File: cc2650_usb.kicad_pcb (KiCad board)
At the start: 2 copper layers, 49.9 x 28 mm, 63 parts, among them P1 CONN_01X07, P2 CONN_01X04, P3 CONN_01X02, P4 CONN_01X08, U1 CC2650F128RHB, X1 24Mhz, Y1 32.768kHz

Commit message: More routing
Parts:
- added C18: 1uF, Capacitors_SMD:C_0603, F.Cu at (141.2, 110.5)
- added C19: 1uF, Capacitors_SMD:C_0603, F.Cu at (146.1, 108.7)
- added D1: USR_LED, LEDs:LED_0603, F.Cu at (120.0, 62.0)
- added D2: PWR_LED, LEDs:LED_0603, F.Cu at (138.6, 108.1)
- added D3: BAT60JFILM, Diodes_SMD:SOD-323, F.Cu at (145.4, 106.3)
- added P5: VBAT, battery_extra:CR2032_SMD, B.Cu at (152.7, 105.1)
- added Q1: FDN340P, TO_SOT_Packages_SMD:SOT-23, F.Cu at (141.6, 105.4)
- added R3: 360R, Resistors_SMD:R_0603, F.Cu at (113.0, 68.2)
- added R4: 360R, Resistors_SMD:R_0603, F.Cu at (138.6, 105.2)
- added R5: 100K, Resistors_SMD:R_0603, F.Cu at (111.9, 82.7)
- added REF**: VIA_0.6mm, GNDVIA:GND_VIA_0.6mm, F.Cu at (146.5, 90.1)
- added REF**: VIA_0.6mm, GNDVIA:GND_VIA_0.6mm, F.Cu at (148.3, 105.3)
- added REF**: VIA_0.6mm, GNDVIA:GND_VIA_0.6mm, F.Cu at (154.5, 90.1)
- added REF**: VIA_0.6mm, GNDVIA:GND_VIA_0.6mm, F.Cu at (168.0, 99.2)
- added REF**: VIA_0.6mm, GNDVIA:GND_VIA_0.6mm, F.Cu at (166.9, 99.2)
- added REF**: VIA_0.6mm, GNDVIA:GND_VIA_0.6mm, F.Cu at (165.7, 99.2)
- added REF**: VIA_0.6mm, GNDVIA:GND_VIA_0.6mm, F.Cu at (166.7, 96.2)
- added REF**: VIA_0.6mm, GNDVIA:GND_VIA_0.6mm, F.Cu at (165.7, 96.2)
- added SW1: RST, smallbutton:SmallButton, F.Cu at (135.7, 87.8)
- added SW2: USR_BTN, smallbutton:SmallButton, F.Cu at (160.6, 75.5)
- added U2: XC6206P332MR, TO_SOT_Packages_SMD:SOT-23, F.Cu at (144.4, 111.2)
- added W1: TEST_1P, Connect:PINTST, F.Cu at (70.9, 88.8)
- moved C5 32.4 mm to (146.3, 91.7), turned to 180 degrees
- moved C7 14.4 mm to (150.6, 73.6)
- moved R1 13.4 mm to (143.0, 90.3)
- moved P3 8.77 mm to (135.7, 111.2)
- moved P4 2.31 mm to (131.8, 92.7)
- moved L1 1.02 mm to (148.5, 92.5)
- moved REF** 0.32 mm to (170.9, 96.2)
- moved REF** 0.12 mm to (167.8, 96.2)
- moved REF** 0.12 mm to (169.3, 96.2)
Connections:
- net /nSRST renamed /~SRST~
- C1 pad 1: +3V3 -> VDDS
- C2 pad 1: +3V3 -> VDDS
- C3 pad 1: +3V3 -> VDDS
- C4 pad 1: +3V3 -> VDDS
- P1 pad 7: +3V3 -> VDDS
- P2 pad 4: +3V3 -> VDDS
- P3 pad 2: +3V3 -> /VEXT
- R1 pad 1: +3V3 -> VDDS
- U1 pad 11: +3V3 -> VDDS
- U1 pad 18: +3V3 -> VDDS
- U1 pad 28: +3V3 -> VDDS
- U1 pad 6: (no net) -> /USR_LED
- U1 pad 7: (no net) -> /USR_BTN
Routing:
- net VDDS: track 0.00 -> 43.7 mm, vias 0 -> 2
- net /DIO_14: track 0.00 -> 26.8 mm
- net /DIO_13: track 0.00 -> 24.6 mm
- net /DIO_12: track 0.00 -> 21.8 mm
- net /DIO_11: track 0.00 -> 20.3 mm
- net /DIO_7: track 0.00 -> 19.8 mm
- net /DIO_10: track 0.00 -> 19.5 mm
- net /DIO_8: track 0.00 -> 18.9 mm
- net /DIO_9: track 0.00 -> 18.6 mm
- net /~SRST~: track 7.55 -> 21.3 mm
- net /VBAT: track 0.00 -> 9.03 mm, vias 0 -> 1
- net VIN: track 0.00 -> 8.70 mm
- net /TDI: track 0.00 -> 7.51 mm
- net /TMS: track 0.00 -> 7.25 mm
- net /TDO: track 0.00 -> 7.22 mm
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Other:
- net class Default: clearance 0.2 -> 0.16; trace_width 0.25 -> 0.2; via_dia 0.8 -> 0.6; via_drill 0.4 -> 0.3
- rule trace_clearance: 0.2 -> 0.16

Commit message: Routing almost done
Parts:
- removed R5: 100K, Resistors_SMD:R_0603
- removed the REF** at (154.2, 99.8)
- removed the REF** at (154.2, 100.9)
- removed the REF** at (152.7, 101.3)
- removed SW2: USR_BTN, smallbutton:SmallButton
- added REF**: VIA_0.6mm, GNDVIA:GND_VIA_0.6mm, F.Cu at (149.1, 102.4)
- added REF**: VIA_0.6mm, GNDVIA:GND_VIA_0.6mm, F.Cu at (138.8, 101.9)
- added REF**: VIA_0.6mm, GNDVIA:GND_VIA_0.6mm, F.Cu at (146.6, 101.0)
- added REF**: VIA_0.6mm, GNDVIA:GND_VIA_0.6mm, F.Cu at (149.9, 108.1)
- added REF**: VIA_0.6mm, GNDVIA:GND_VIA_0.6mm, F.Cu at (155.0, 112.3)
- added REF**: VIA_0.6mm, GNDVIA:GND_VIA_0.6mm, F.Cu at (153.4, 110.1)
- added REF**: VIA_0.6mm, GNDVIA:GND_VIA_0.6mm, F.Cu at (160.2, 112.3)
- added REF**: VIA_0.6mm, GNDVIA:GND_VIA_0.6mm, F.Cu at (159.3, 109.8)
- added REF**: VIA_0.6mm, GNDVIA:GND_VIA_0.6mm, F.Cu at (168.8, 111.8)
- added REF**: VIA_0.6mm, GNDVIA:GND_VIA_0.6mm, F.Cu at (163.2, 110.6)
- added REF**: VIA_0.6mm, GNDVIA:GND_VIA_0.6mm, F.Cu at (167.4, 109.5)
- added REF**: VIA_0.6mm, GNDVIA:GND_VIA_0.6mm, F.Cu at (151.2, 100.4)
- added REF**: VIA_0.6mm, GNDVIA:GND_VIA_0.6mm, F.Cu at (171.3, 107.9)
- added REF**: VIA_0.6mm, GNDVIA:GND_VIA_0.6mm, F.Cu at (165.2, 106.5)
- added REF**: VIA_0.6mm, GNDVIA:GND_VIA_0.6mm, F.Cu at (164.9, 102.1)
- added REF**: VIA_0.6mm, GNDVIA:GND_VIA_0.6mm, F.Cu at (160.2, 103.7)
- added REF**: VIA_0.6mm, GNDVIA:GND_VIA_0.6mm, F.Cu at (148.1, 110.9)
- added REF**: VIA_0.6mm, GNDVIA:GND_VIA_0.6mm, F.Cu at (142.6, 108.5)
- added REF**: VIA_0.6mm, GNDVIA:GND_VIA_0.6mm, F.Cu at (135.2, 108.2)
- added REF**: VIA_0.6mm, GNDVIA:GND_VIA_0.6mm, F.Cu at (144.1, 101.7)
- added REF**: VIA_0.6mm, GNDVIA:GND_VIA_0.6mm, F.Cu at (144.0, 98.2)
- added REF**: VIA_0.6mm, GNDVIA:GND_VIA_0.6mm, F.Cu at (143.0, 91.8)
- added REF**: VIA_0.6mm, GNDVIA:GND_VIA_0.6mm, F.Cu at (150.3, 89.3)
- added REF**: VIA_0.6mm, GNDVIA:GND_VIA_0.6mm, F.Cu at (162.0, 90.2)
- added REF**: VIA_0.6mm, GNDVIA:GND_VIA_0.6mm, F.Cu at (159.2, 93.2)
- added REF**: VIA_0.6mm, GNDVIA:GND_VIA_0.6mm, F.Cu at (161.8, 93.3)
- added REF**: VIA_0.6mm, GNDVIA:GND_VIA_0.6mm, F.Cu at (160.9, 101.7)
- added REF**: VIA_0.6mm, GNDVIA:GND_VIA_0.6mm, F.Cu at (157.0, 103.7)
- added REF**: VIA_0.6mm, GNDVIA:GND_VIA_0.6mm, F.Cu at (154.8, 104.7)
- added REF**: VIA_0.6mm, GNDVIA:GND_VIA_0.6mm, F.Cu at (133.9, 88.1)
- added REF**: VIA_0.6mm, GNDVIA:GND_VIA_0.6mm, F.Cu at (138.3, 91.4)
- added REF**: VIA_0.6mm, GNDVIA:GND_VIA_0.6mm, F.Cu at (138.7, 95.2)
- added REF**: VIA_0.6mm, GNDVIA:GND_VIA_0.6mm, F.Cu at (134.3, 96.8)
- added REF**: VIA_0.6mm, GNDVIA:GND_VIA_0.6mm, F.Cu at (134.2, 99.2)
- added REF**: VIA_0.6mm, GNDVIA:GND_VIA_0.6mm, F.Cu at (136.8, 99.3)
- moved W1 77.4 mm to (148.2, 90.5)
- moved R3 57.3 mm to (164.3, 93.9), turned to 90 degrees
- moved D1 55.9 mm to (165.9, 93.9), turned to 270 degrees
- moved C1 55.0 mm to (151.4, 102.4), turned to 90 degrees
- moved C2 45.3 mm to (154.5, 92.4)
- moved C4 40.9 mm to (146.4, 93.9)
- moved C3 40.6 mm to (144.2, 94.0), turned to 90 degrees
- moved C12 36.8 mm to (144.9, 96.2), turned to 180 degrees
- moved C7 28.9 mm to (153.7, 102.4), turned to 270 degrees
- moved C6 22.7 mm to (154.1, 90.5)
- moved C9 6.57 mm to (155.7, 107.2)
- moved C10 6.32 mm to (162.0, 106.0)
- moved X1 6.32 mm to (159.1, 106.1)
- moved C8 4.24 mm to (159.2, 101.8), turned to 90 degrees
- moved REF** 2.20 mm to (156.7, 89.9)
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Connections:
- net Net-(C6-Pad1) renamed /DCOUPL
- U1 pad 7: /USR_BTN -> (no net)
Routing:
- net VDDR: track 3.03 -> 50.8 mm, vias 0 -> 2
- net VDDS: track 43.7 -> 58.5 mm, vias 2 -> 3
- net /USR_LED: track 0.00 -> 10.7 mm, vias 0 -> 2
- net /X24M_P: track 6.40 -> 11.5 mm
- net /~SRST~: track 21.3 -> 25.0 mm, vias 1 -> 2
- net /DCOUPL: track 0.00 -> 3.37 mm
- net /X24M_N: track 8.29 -> 11.5 mm
- net Net-(D1-Pad2): track 0.00 -> 1.64 mm
- net /VBAT: track 9.03 -> 10.6 mm
- net /DIO_14: track 26.8 -> 25.6 mm
- net /DIO_9: track 18.6 -> 19.7 mm
- net /DIO_10: track 19.5 -> 20.6 mm
- net /DIO_11: track 20.3 -> 21.4 mm
- net Net-(D2-Pad2): track 1.39 -> 2.39 mm
- net /DIO_13: track 24.6 -> 23.6 mm
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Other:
- net class Antenna: clearance 0.2 -> 0.15
- net class Default: clearance 0.16 -> 0.15
- net class Power: clearance 0.2 -> 0.15; trace_width 0.4 -> 0.35
- rule trace_clearance: 0.16 -> 0.15
- rule via_min_size: 0.4 -> 0.6
- board text added: "DIO_10"
- board text added: "DIO_11"
- board text added: "DIO_7"
- board text added: "DIO_8"
- board text added: "DIO_9"

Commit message: More routing, remove useless TP
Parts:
- removed the REF** at (151.2, 100.4)
- removed the REF** at (162.0, 90.2)
- removed W1: TEST_1P, Connect:PINTST
- added REF**: VIA_0.6mm, GNDVIA:GND_VIA_0.6mm, F.Cu at (163.2, 105.7)
- added REF**: VIA_0.6mm, GNDVIA:GND_VIA_0.6mm, F.Cu at (167.0, 100.6)
- added REF**: VIA_0.6mm, GNDVIA:GND_VIA_0.6mm, F.Cu at (164.4, 104.3)
- added REF**: VIA_0.6mm, GNDVIA:GND_VIA_0.6mm, F.Cu at (171.1, 103.9)
- added REF**: VIA_0.6mm, GNDVIA:GND_VIA_0.6mm, F.Cu at (162.8, 89.9)
- added REF**: VIA_0.6mm, GNDVIA:GND_VIA_0.6mm, F.Cu at (149.8, 91.3)
- added REF**: VIA_0.6mm, GNDVIA:GND_VIA_0.6mm, F.Cu at (156.7, 101.1)
- moved REF** 1.40 mm to (160.1, 108.6)
- moved C1 0.34 mm to (151.1, 102.4)
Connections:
- U1 pad 10: (no net) -> Net-(U1-Pad10)
- U1 pad 3: (no net) -> Net-(U1-Pad3)
- U1 pad 7: (no net) -> Net-(U1-Pad7)
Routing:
- net VDDR: track 50.8 -> 55.6 mm
- net GND: track 4.63 -> 0.00 mm
- net VDDS: track 58.5 -> 59.9 mm

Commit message: Routing done
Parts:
- added REF**: VIA_0.6mm, GNDVIA:GND_VIA_0.6mm, F.Cu at (164.7, 112.5)
- added REF**: VIA_0.6mm, GNDVIA:GND_VIA_0.6mm, F.Cu at (135.1, 90.5)
- added REF**: VIA_0.6mm, GNDVIA:GND_VIA_0.6mm, F.Cu at (137.1, 88.8)
- added REF**: VIA_0.6mm, GNDVIA:GND_VIA_0.6mm, F.Cu at (139.5, 89.4)
- added REF**: VIA_0.6mm, GNDVIA:GND_VIA_0.6mm, F.Cu at (140.3, 93.2)
- added REF**: VIA_0.6mm, GNDVIA:GND_VIA_0.6mm, F.Cu at (135.8, 92.6)
- added REF**: VIA_0.6mm, GNDVIA:GND_VIA_0.6mm, F.Cu at (141.0, 101.7)
- added REF**: VIA_0.6mm, GNDVIA:GND_VIA_0.6mm, F.Cu at (167.7, 104.5)
- added REF**: VIA_0.6mm, GNDVIA:GND_VIA_0.6mm, F.Cu at (168.6, 102.9)
- added REF**: VIA_0.6mm, GNDVIA:GND_VIA_0.6mm, F.Cu at (168.4, 106.4)
- added REF**: VIA_0.6mm, GNDVIA:GND_VIA_0.6mm, F.Cu at (171.0, 88.5)
- added REF**: VIA_0.6mm, GNDVIA:GND_VIA_0.6mm, F.Cu at (157.4, 111.3)
- added REF**: VIA_0.6mm, GNDVIA:GND_VIA_0.6mm, F.Cu at (169.4, 90.1)
- added REF**: VIA_0.6mm, GNDVIA:GND_VIA_0.6mm, F.Cu at (167.1, 90.1)
- added REF**: VIA_0.6mm, GNDVIA:GND_VIA_0.6mm, F.Cu at (165.9, 91.3)
- added REF**: VIA_0.6mm, GNDVIA:GND_VIA_0.6mm, F.Cu at (168.5, 91.4)
- added REF**: VIA_0.6mm, GNDVIA:GND_VIA_0.6mm, F.Cu at (170.6, 91.3)
- added REF**: VIA_0.6mm, GNDVIA:GND_VIA_0.6mm, F.Cu at (168.9, 92.9)
- added REF**: VIA_0.6mm, GNDVIA:GND_VIA_0.6mm, F.Cu at (170.8, 93.0)
- added REF**: VIA_0.6mm, GNDVIA:GND_VIA_0.6mm, F.Cu at (170.1, 94.8)
- added REF**: VIA_0.6mm, GNDVIA:GND_VIA_0.6mm, F.Cu at (167.9, 94.2)
- added REF**: VIA_0.6mm, GNDVIA:GND_VIA_0.6mm, F.Cu at (151.0, 111.9)
- added REF**: VIA_0.6mm, GNDVIA:GND_VIA_0.6mm, F.Cu at (132.6, 112.5)
- added REF**: VIA_0.6mm, GNDVIA:GND_VIA_0.6mm, F.Cu at (137.9, 108.8)
- added REF**: VIA_0.6mm, GNDVIA:GND_VIA_0.6mm, F.Cu at (141.5, 112.7)
- added REF**: VIA_0.6mm, GNDVIA:GND_VIA_0.6mm, F.Cu at (132.9, 89.6)
- added REF**: VIA_0.6mm, GNDVIA:GND_VIA_0.6mm, F.Cu at (130.9, 89.8)
- added REF**: VIA_0.6mm, GNDVIA:GND_VIA_0.6mm, F.Cu at (136.5, 87.0)
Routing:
- net VDDS: track 59.9 -> 80.9 mm
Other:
- net class Antenna: via_dia 0.8 -> 0.6; via_drill 0.4 -> 0.3
- net class Power: via_dia 0.8 -> 0.6; via_drill 0.4 -> 0.3

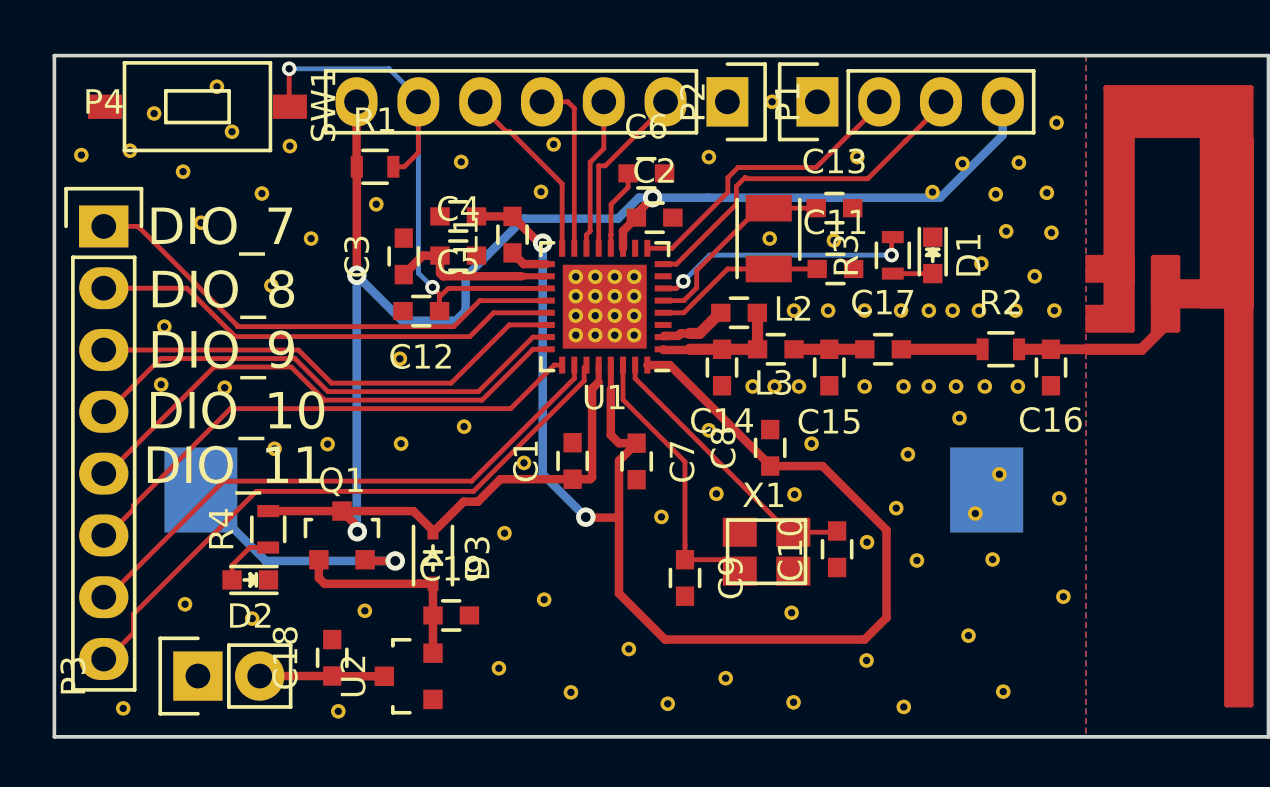
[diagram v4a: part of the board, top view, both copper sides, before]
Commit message: Fully routed, fancy corners
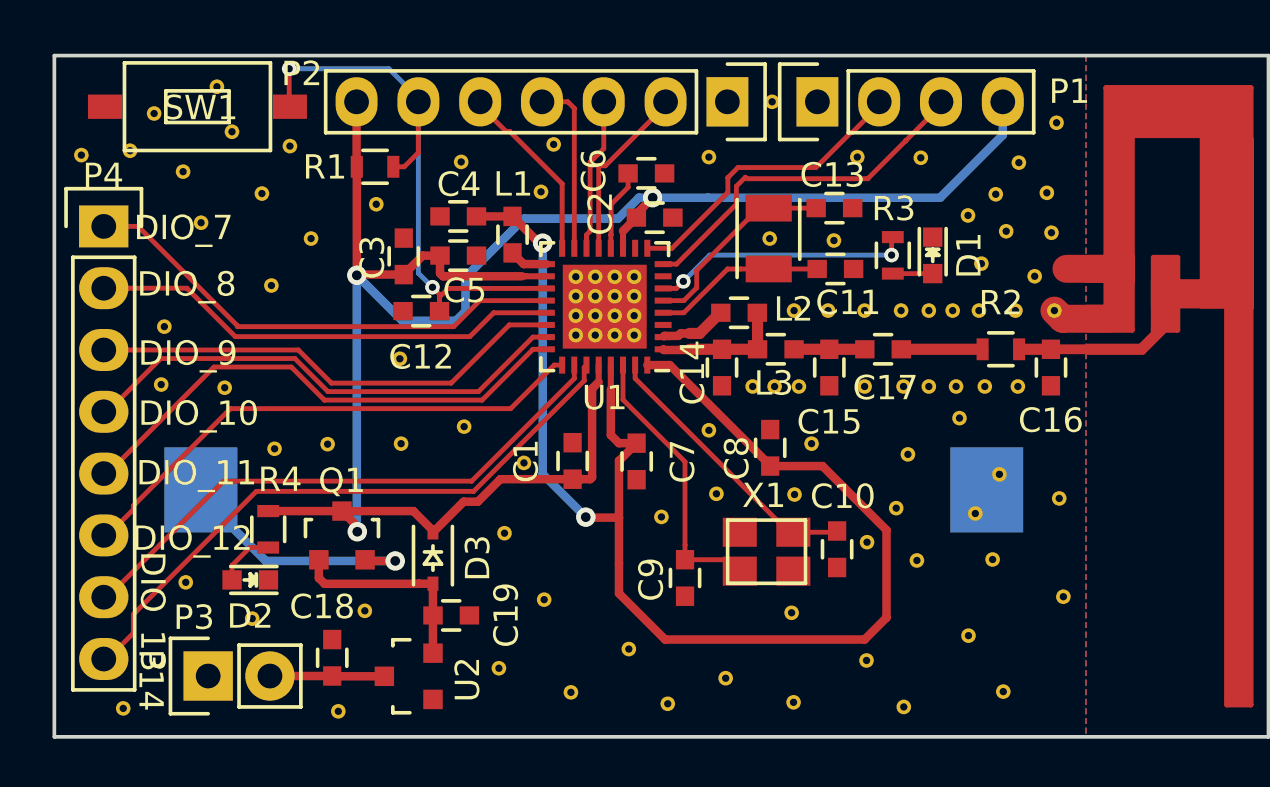
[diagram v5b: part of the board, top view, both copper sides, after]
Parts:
- moved REF** 2.14 mm to (167.3, 92.3)
- moved REF** 1.49 mm to (165.4, 89.9)
- moved REF** 0.90 mm to (135.2, 107.3)
- moved P3 0.42 mm to (136.1, 111.2)
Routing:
- net GND: track 0.00 -> 4.17 mm
- net VDDS: track 80.9 -> 82.8 mm
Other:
- board text added: "DIO_12"
- board text added: "DIO_13"
- board text added: "P14"

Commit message: Stuff
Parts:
- moved REF** 4.80 mm to (140.3, 95.1)
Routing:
- net /DIO_10: track 20.6 -> 20.0 mm
- net /DIO_11: track 21.4 -> 20.9 mm
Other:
- outline, holes or cut-outs redrawn
- board text added: "+"
- board text added: "-"
